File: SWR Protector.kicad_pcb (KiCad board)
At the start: 2 copper layers, 27 parts, among them J1 Barrel_Jack, J2 Barrel_Jack, J3 transceiver, J4 antenna, K2 ATX209, Q1 2N3904, T1 1:12, T2 12:1 ???, U1 LM78L05_TO92, U2 LM358

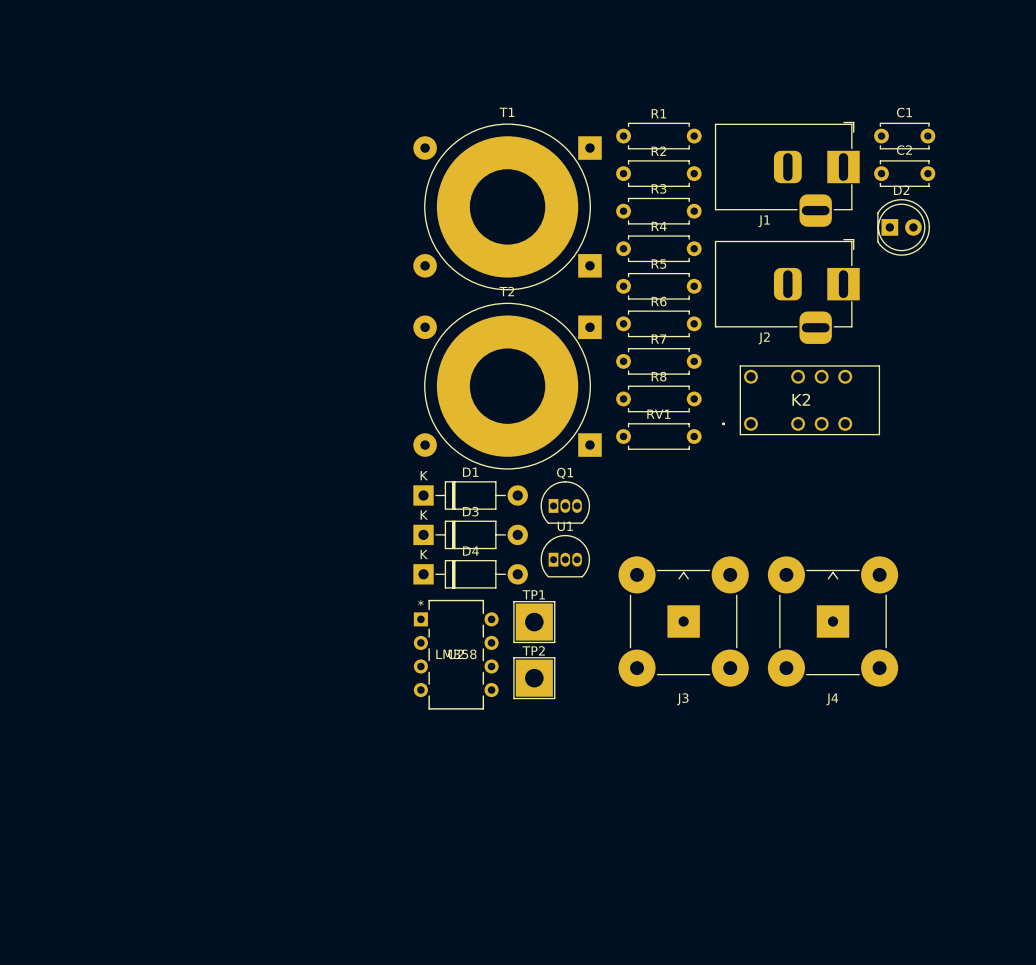
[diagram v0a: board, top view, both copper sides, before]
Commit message: placed parts on PCB and wired them up.  DRC reports zero errors and a handful of warnings about overlapping silk screen.
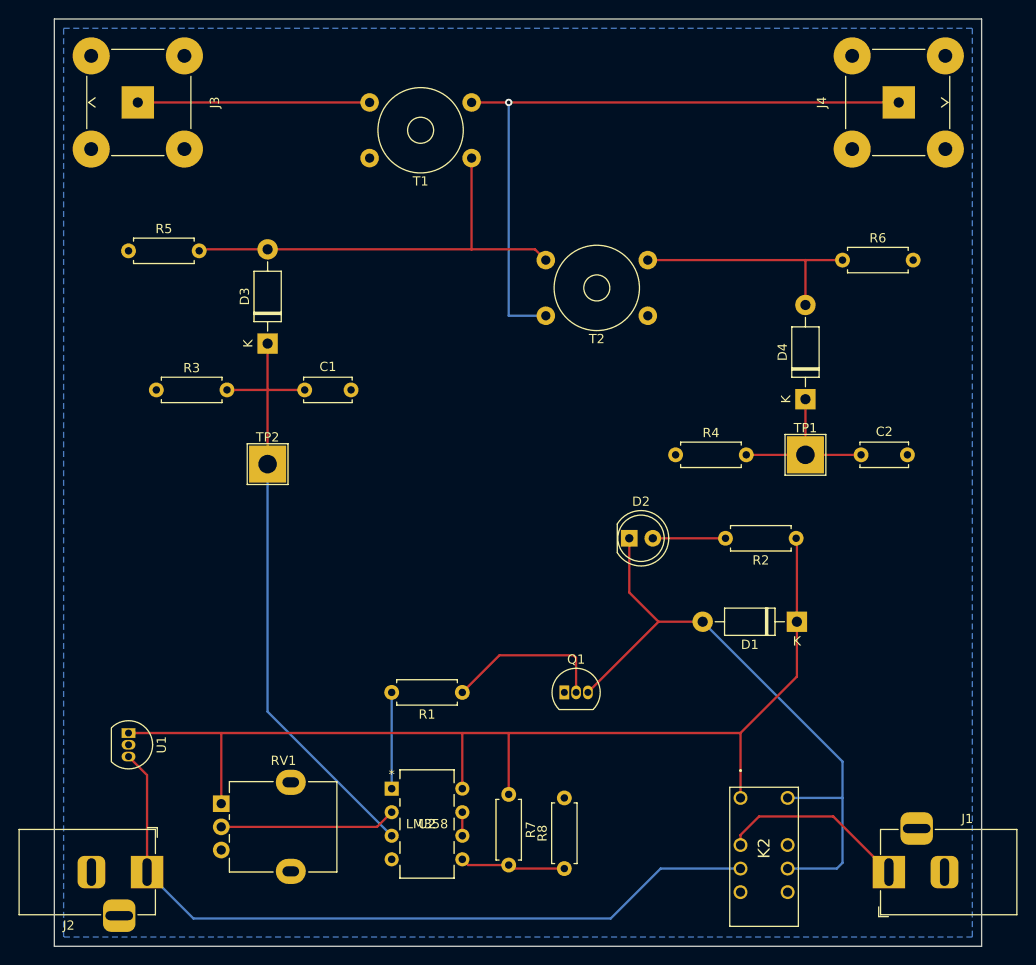
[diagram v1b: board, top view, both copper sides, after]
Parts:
- RV1: footprint Resistor_THT:R_Axial_DIN0207_L6.3mm_D2.5mm_P7.62mm_Horizontal -> Potentiometer_THT:Potentiometer_Alpha_RD901F-40-00D_Single_Vertical
- T1, T2: footprint Transformer_THT:Transformer_Toroid_Horizontal_D18.0mm -> Transformer_THT:Transformer_Toroid_Horizontal_D9.0mm_Amidon-T30
- moved J2 98.3 mm to (95.0, 139.0)
- moved J3 81.2 mm to (94.0, 56.0), turned to 90 degrees
- moved J1 76.2 mm to (175.0, 139.0), turned to 180 degrees
- moved C1 68.0 mm to (112.0, 87.0)
- moved R1 62.5 mm to (129.0, 119.6), turned to 180 degrees
- moved RV1 58.7 mm to (103.0, 131.6)
- moved J4 56.4 mm to (176.1, 56.0), turned to -90 degrees
- moved R3 53.9 mm to (96.0, 87.0)
- moved R5 53.5 mm to (93.0, 72.0)
- moved R8 51.0 mm to (140.0, 138.6), turned to 90 degrees
- moved U1 49.5 mm to (93.0, 124.0), turned to -90 degrees
- moved R7 48.3 mm to (134.0, 130.6), turned to -90 degrees
- moved D4 45.3 mm to (166.0, 88.0), turned to 90 degrees
- moved D2 43.7 mm to (147.0, 103.0)
- moved R2 43.5 mm to (165.0, 103.0), turned to 180 degrees
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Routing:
- net +5V: track 0.00 -> 116.8 mm
- net +12V: track 0.00 -> 81.6 mm
- net Net-(J4-In): track 0.00 -> 73.1 mm, vias 0 -> 1
- net Net-(D1-A): track 0.00 -> 70.2 mm
- net Net-(D3-K): track 0.00 -> 67.0 mm
- net Net-(D3-A): track 0.00 -> 47.8 mm
- net Net-(D4-A): track 0.00 -> 25.8 mm
- net Net-(J3-In): track 0.00 -> 25.0 mm
- net Net-(K2-NC_1): track 0.00 -> 20.4 mm
- net Net-(U2A--): track 0.00 -> 19.0 mm
- net Net-(D4-K): track 0.00 -> 18.4 mm
- net Net-(Q1-B): track 0.00 -> 17.8 mm
- net Net-(U2B-+): track 0.00 -> 11.4 mm
- net Net-(R1-Pad2): track 0.00 -> 10.4 mm
- net Net-(D2-A): track 0.00 -> 7.84 mm
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- added copper zone on B.Cu, net GND
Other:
- board outline added: 100 x 100 mm

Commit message: After review with Ron, lots of changes to make. Updates readme.txt with lots of notes TODO. Started playing with net classes as I need wider traces. 1mm for default trace, and 2.5mm for +12v power traces.
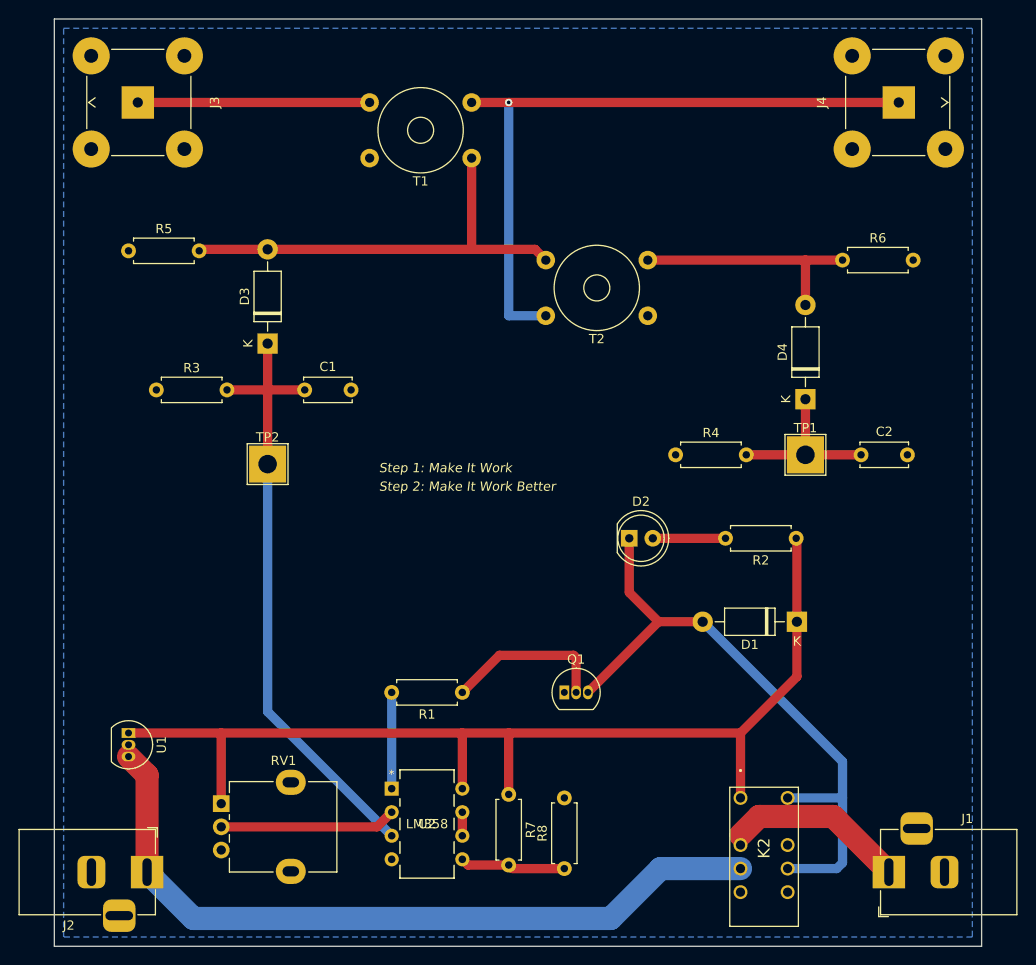
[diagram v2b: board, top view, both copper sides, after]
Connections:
- J1 pad 1: Net-(K2-NC_1) -> +12V
- K2 pad 3: Net-(K2-NC_1) -> +12V
- U1 pad 2: GND -> +12V
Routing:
- net Net-(K2-NC_1): track 20.4 -> 0.00 mm
- net +12V: track 81.6 -> 100.9 mm
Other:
- board text added: "Step 1: Make It Work"
- board text added: "Step 2: Make It Work Better"

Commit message: Wider traces done.  FT37-43 oriented vertically with new footprint.
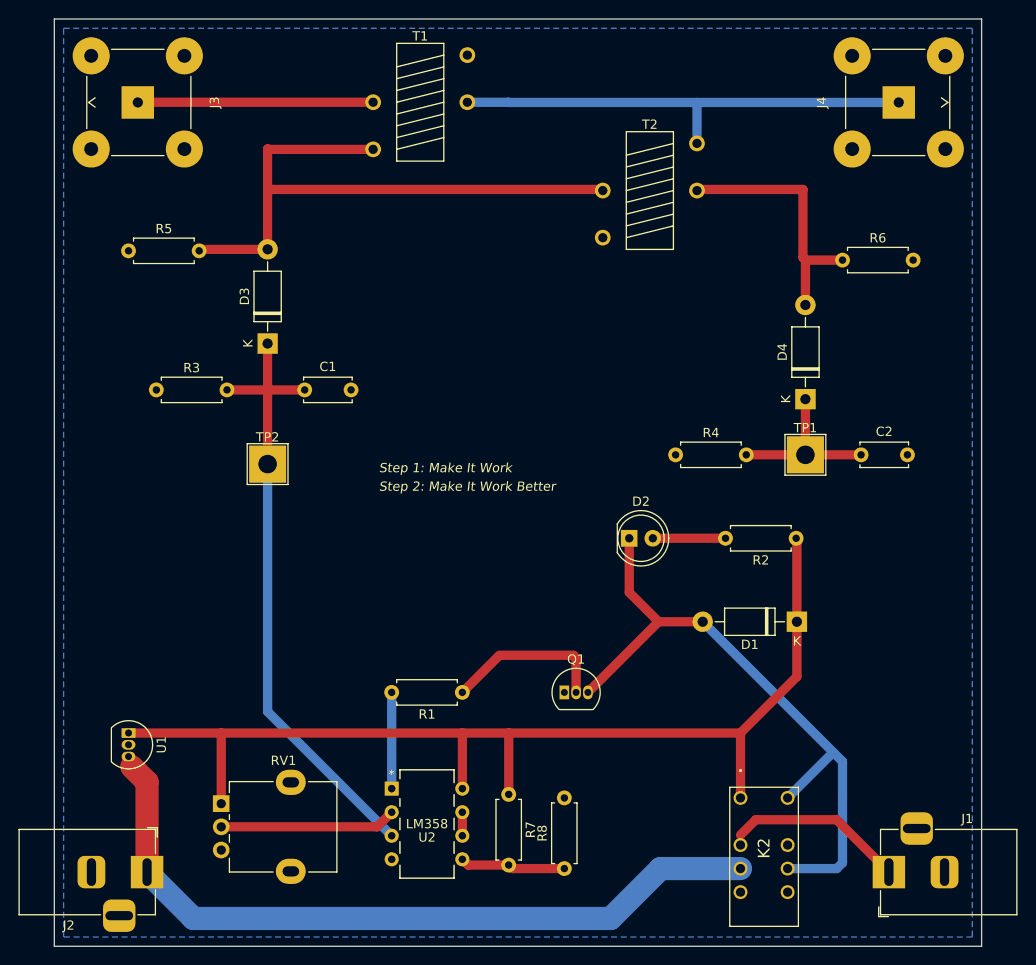
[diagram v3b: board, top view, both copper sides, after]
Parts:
- T1: footprint Transformer_THT:Transformer_Toroid_Horizontal_D9.0mm_Amidon-T30 -> FT37-43:FT37-43-TRANSFORMER
- T2: value 12:1 ??? -> 1:12; footprint Transformer_THT:Transformer_Toroid_Horizontal_D9.0mm_Amidon-T30 -> FT37-43:FT37-43-TRANSFORMER
- moved T2 15.1 mm to (149.2, 57.9), turned to 0 degrees
- moved T1 9.44 mm to (124.5, 48.4), turned to 0 degrees
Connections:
- J1 pad 1: +12V -> Net-(K2-NC_1)
- K2 pad 3: +12V -> Net-(K2-NC_1)
- T1 pad 1: Net-(J4-In) -> GND
- T1 pad 2: Net-(J3-In) -> Net-(D3-A)
- T1 pad 3: Net-(D3-A) -> Net-(J4-In)
- T1 pad 4: GND -> Net-(J3-In)
- T2 pad 1: Net-(D4-A) -> Net-(J4-In)
- T2 pad 2: Net-(D3-A) -> GND
- T2 pad 3: GND -> Net-(D4-A)
- T2 pad 4: Net-(J4-In) -> Net-(D3-A)
- U1 pad 2: +12V -> GND
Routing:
- net Net-(J4-In): track 73.1 -> 51.0 mm, vias 1 -> 0
- net +12V: track 100.9 -> 80.4 mm
- net Net-(K2-NC_1): track 0.00 -> 19.0 mm
- net Net-(D3-A): track 47.8 -> 65.6 mm
- net Net-(D4-A): track 25.8 -> 28.2 mm
- net Net-(D1-A): track 70.2 -> 71.3 mm

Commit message: moved transceiver BNC jack to the same side of the board as the switched pwr
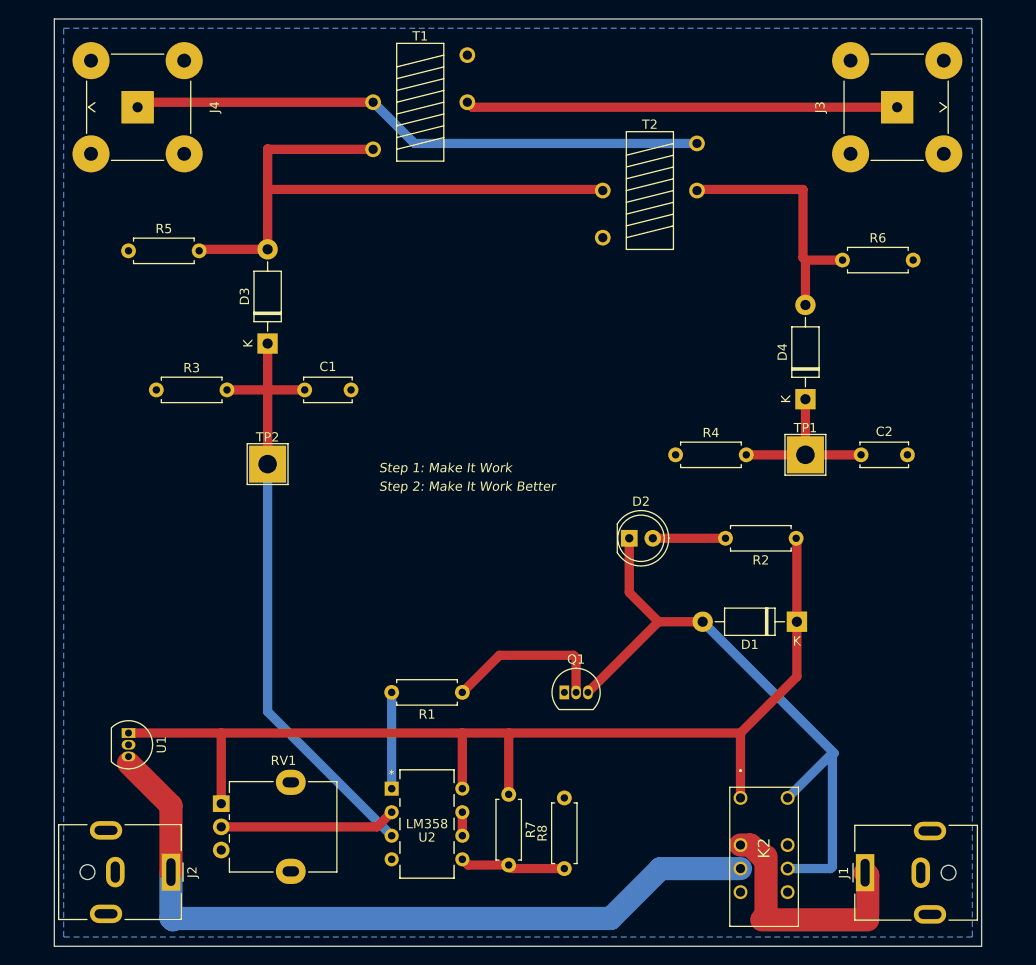
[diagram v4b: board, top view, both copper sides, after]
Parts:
- J1, J2: footprint Connector_BarrelJack:BarrelJack_Horizontal -> Connector_BarrelJack:BarrelJack_CUI_PJ-063AH_Horizontal
- moved J4 82.1 mm to (94.0, 56.5), turned to 90 degrees
- moved J3 81.9 mm to (175.9, 56.5), turned to -90 degrees
- moved J2 2.58 mm to (97.6, 139.0), turned to -90 degrees
- moved J1 2.57 mm to (172.4, 139.1), turned to 90 degrees
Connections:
- T1 pad 3: Net-(J4-In) -> Net-(J3-In)
- T1 pad 4: Net-(J3-In) -> Net-(J4-In)
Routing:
- net Net-(J3-In): track 25.4 -> 46.6 mm
- net Net-(J4-In): track 51.0 -> 62.4 mm
- net Net-(K2-NC_1): track 19.0 -> 25.0 mm
- net +12V: track 80.4 -> 82.4 mm
- net Net-(D1-A): track 71.3 -> 70.1 mm
